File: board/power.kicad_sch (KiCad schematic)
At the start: 43 parts, among them Q1 BSS138, Q2 BSS138, Q3 BSS138, Q4 BSS138, Q5 BSS138, Q6 BSS138, Q7 BSS138, Q8 BSS138, Q9 BSS138, U1 OKI-78SR-5_1.5-W36H-C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

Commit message: switched soil sensor ports and layout work
soil sensor ports in fact needed to be the way they were originally after looking into the sensors we are using. Also started moving different components on layout to their spots.
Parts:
- U4: footprint Converter_DCDC:Converter_DCDC_Murata_OKI-78SR_Horizontal -> MRDT_Devices:OKI_Horizontal
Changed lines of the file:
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@@
 			)
 		)
-		(property "Footprint" "Converter_DCDC:Converter_DCDC_Murata_OKI-78SR_Horizontal"
+		(property "Footprint" "MRDT_Devices:OKI_Horizontal"
 			(at 157.48 45.72 0)
 			(effects

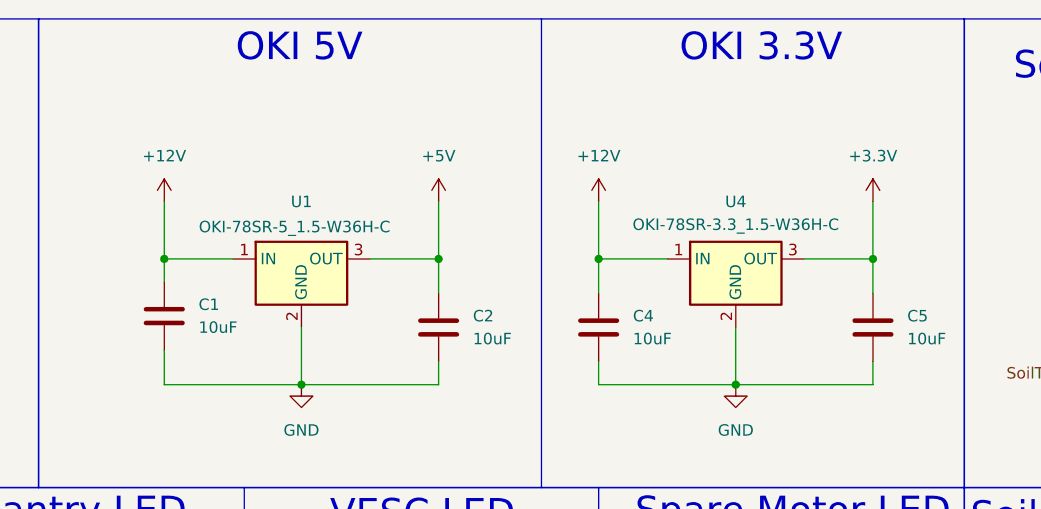
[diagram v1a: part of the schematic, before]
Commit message: Layout Progress
Made a basic setup for locations, placed preliminary wires and text, rearranged teensy pins for simplicity
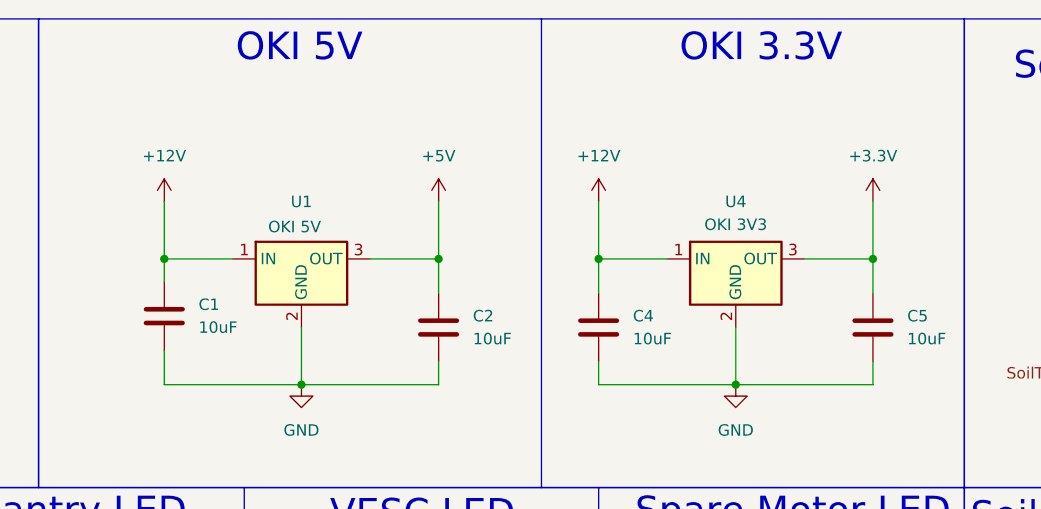
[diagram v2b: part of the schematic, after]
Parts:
- C4, C5: footprint (none) -> Capacitor_SMD:C_0603_1608Metric_Pad1.08x0.95mm_HandSolder
- U1: value OKI-78SR-5_1.5-W36H-C -> OKI 5V
- U4: value OKI-78SR-3.3_1.5-W36H-C -> OKI 3V3
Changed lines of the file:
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@@
 			)
 		)
-		(property "Value" "OKI-78SR-5_1.5-W36H-C"
+		(property "Value" "OKI 5V"
 			(at 107.188 35.814 0)
 			(effects
@@
 			)
 		)
-		(property "Value" "OKI-78SR-3.3_1.5-W36H-C"
+		(property "Value" "OKI 3V3"
 			(at 156.21 35.56 0)
 			(effects
@@
 			)
 		)
-		(property "Footprint" ""
+		(property "Footprint" "Capacitor_SMD:C_0603_1608Metric_Pad1.08x0.95mm_HandSolder"
 			(at 141.9352 50.8 0)
 			(effects
@@
 			)
 		)
-		(property "Footprint" ""
+		(property "Footprint" "Capacitor_SMD:C_0603_1608Metric_Pad1.08x0.95mm_HandSolder"
 			(at 172.4152 50.8 0)
 			(effects

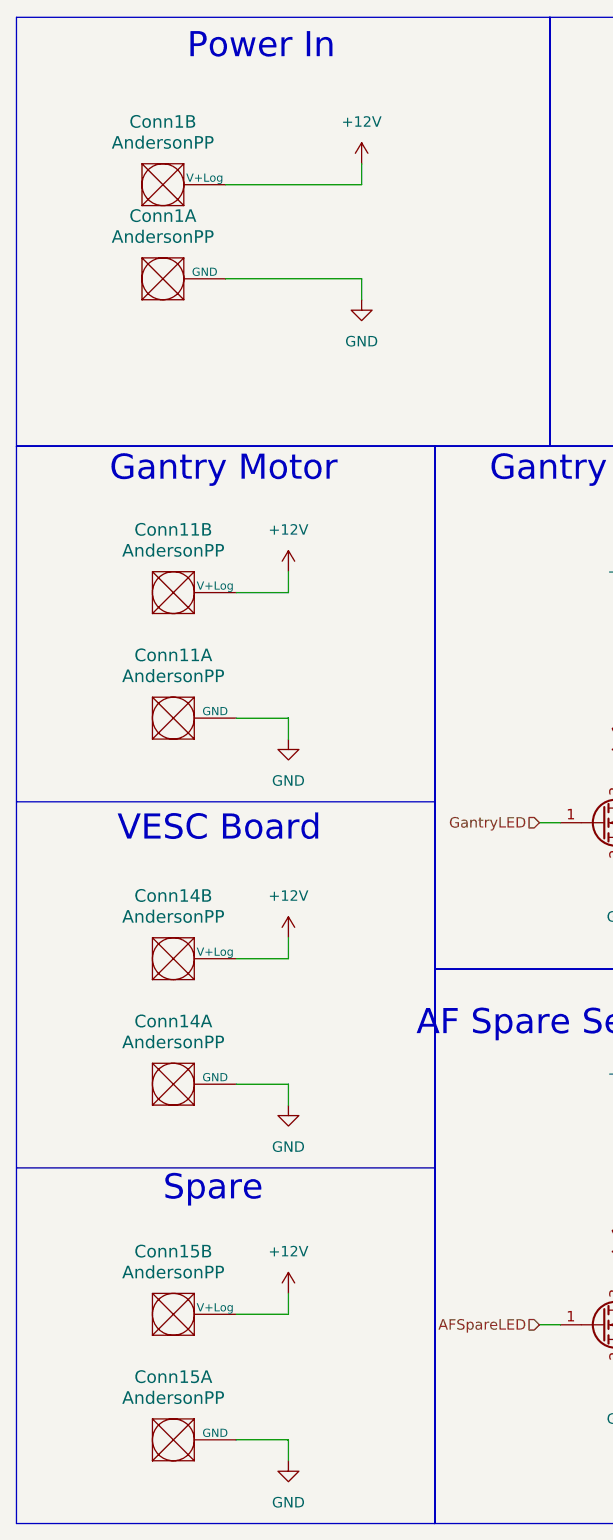
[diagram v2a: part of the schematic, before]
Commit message: Redid layout to shrink & add new power connectors
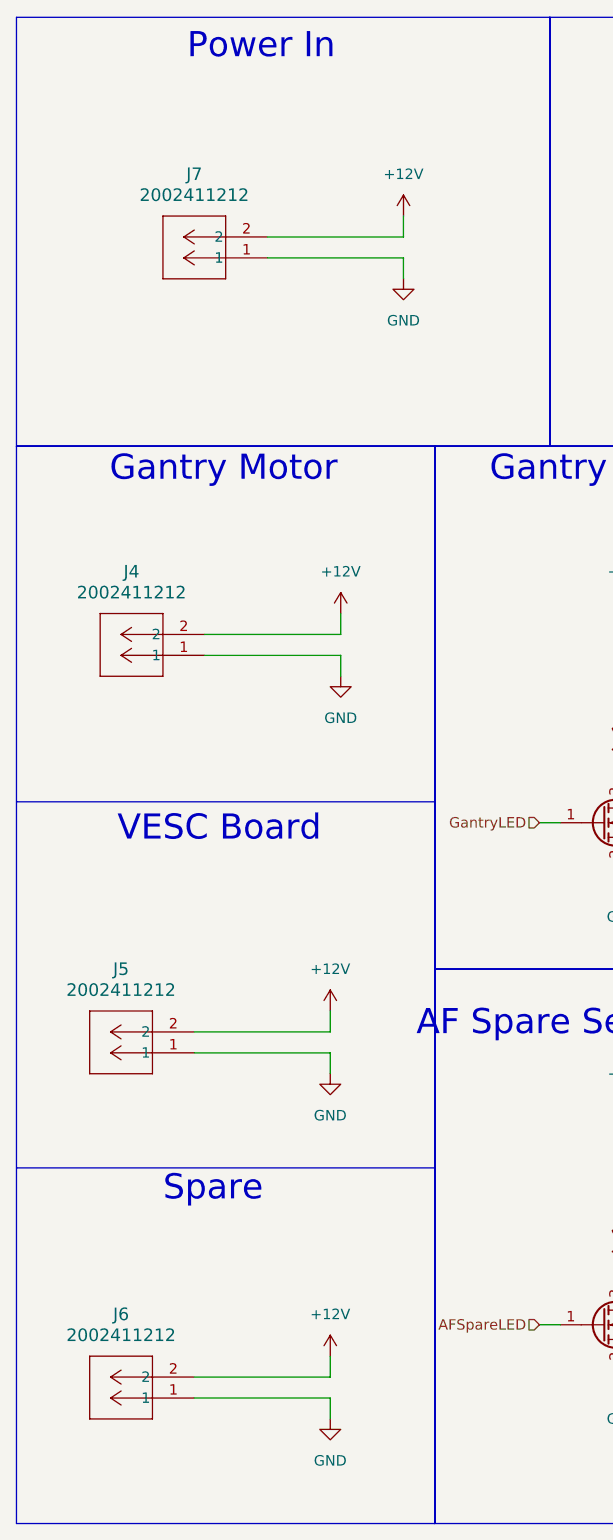
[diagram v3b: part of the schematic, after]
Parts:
- removed Conn1, Conn11, Conn14, Conn15: AndersonPP, MRDT_Connectors:Square_Anderson_2_H_Side_By_Side_PV, symbol MRDT_Connectors:AndersonPP
- added J4, J5, J6, J7: 2002411212, footprints:CONN_2002412000_02_MOL, symbol 2025-11-04_23-05-57:2002411212
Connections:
- net +12V: now also J4.2, J5.2, J6.2, J7.2
- net GND: now also J4.1, J5.1, J6.1, J7.1

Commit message: fine tuning
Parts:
- J4, J5, J6, J7: footprint footprints:CONN_2002412000_02_MOL -> footprints:CONN_SD-76825-0100_02_MOL
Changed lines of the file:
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@@
 			)
 		)
-		(property "Footprint" "footprints:CONN_2002412000_02_MOL"
+		(property "Footprint" "footprints:CONN_SD-76825-0100_02_MOL"
 			(at 35.56 180.34 0)
 			(effects
@@
 			)
 		)
-		(property "Footprint" "footprints:CONN_2002412000_02_MOL"
+		(property "Footprint" "footprints:CONN_SD-76825-0100_02_MOL"
 			(at 36.83 90.17 0)
 			(effects
@@
 			)
 		)
-		(property "Footprint" "footprints:CONN_2002412000_02_MOL"
+		(property "Footprint" "footprints:CONN_SD-76825-0100_02_MOL"
 			(at 44.45 41.91 0)
 			(effects
@@
 			)
 		)
-		(property "Footprint" "footprints:CONN_2002412000_02_MOL"
+		(property "Footprint" "footprints:CONN_SD-76825-0100_02_MOL"
 			(at 35.56 138.43 0)
 			(effects

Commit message: added pin for AF, added gimbal names, refined look
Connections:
- net SpareServoLED1 renamed GimbalPanLED
- net SpareServoLED2 renamed GimbalTiltLED
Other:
- note added: "Gimbal Pan LED"
- note added: "Gimbal Tilt LED"
- note removed: "Spare Servo LED"
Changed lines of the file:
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@@
 		)
 	)
-	(text "Spare Servo LED"
+	(text "Gimbal Tilt LED"
 		(exclude_from_sim no)
 		(at 125.222 134.366 0)
@@
 		)
 	)
-	(text "Spare Servo LED"
+	(text "Gimbal Pan LED"
 		(exclude_from_sim no)
 		(at 251.206 68.326 0)
@@
 		)
 	)
-	(hierarchical_label "SpareServoLED2"
+	(hierarchical_label "GimbalTiltLED"
 		(shape input)
 		(at 121.92 170.18 180)
@@
 		)
 	)
-	(hierarchical_label "SpareServoLED1"
+	(hierarchical_label "GimbalPanLED"
 		(shape input)
 		(at 247.65 109.22 180)

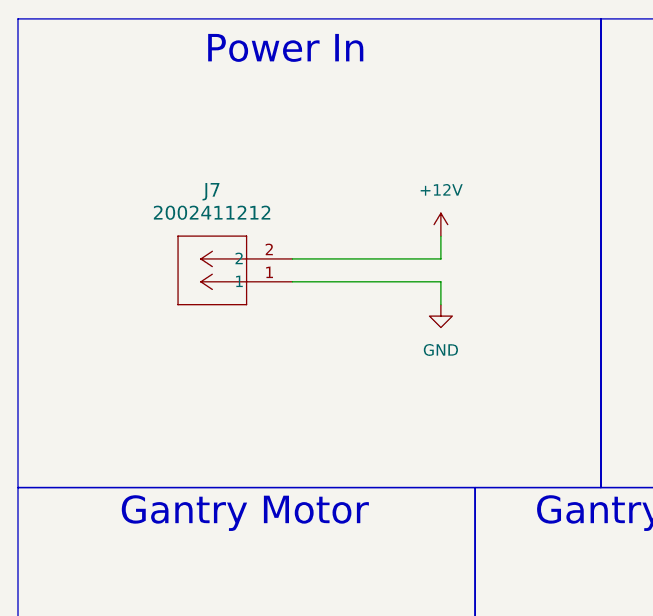
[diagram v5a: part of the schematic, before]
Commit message: Add reverse voltage protection circuit
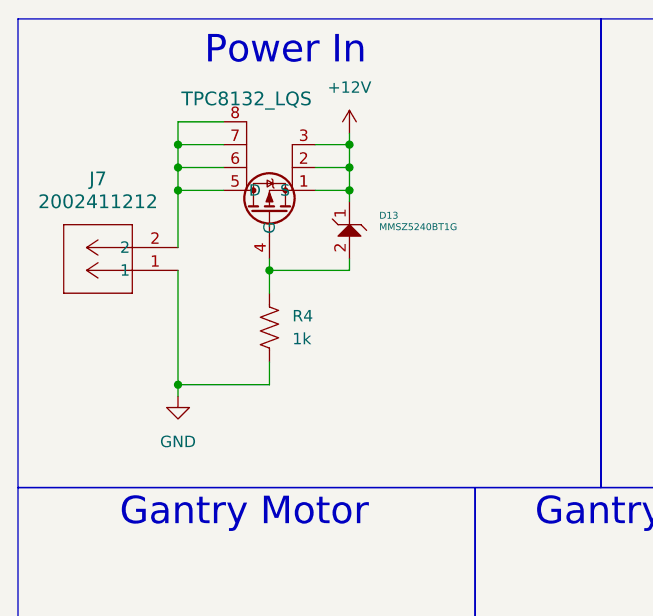
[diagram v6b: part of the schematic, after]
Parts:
- added D13: MMSZ5240BT1G, MRDT_Devices:SOD-123_ONS-L, symbol MRDT_Devices:MMSZ5240BT1G
- added MOSFET1: TPC8132_LQS, MRDT_Devices:SOP-8_TOS-L, symbol MRDT_Devices:TPC8132_LQS
- added R4: 1k, Resistor_SMD:R_0603_1608Metric_Pad0.98x0.95mm_HandSolder, symbol Device:R_US
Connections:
- net +12V: now also D13.1, MOSFET1.1 (S), MOSFET1.2, MOSFET1.3; no longer J7.2
- net GND: now also R4.2
- new net: D13.2, MOSFET1.4 (G), R4.1
- new net: J7.2, MOSFET1.5 (D), MOSFET1.6, MOSFET1.7, MOSFET1.8
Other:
- moved on the sheet: J7

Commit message: Redesigning Layout
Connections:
- net AFSpareLED renamed SpareLED2
- net CacheSpareLED renamed SpareLED1
- net SpareMotorLED renamed Spare12VLED
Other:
- note added: "Spare 12V LED"
- note added: "Spare LED 1"
- note added: "Spare LED 2"
- note removed: "AF Spare Servo LED"
- note removed: "Soil Cache Spare LED"
- note removed: "Spare Motor LED"
